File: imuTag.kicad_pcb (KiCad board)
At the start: 4 copper layers, 41.3 x 40 mm, 44 parts, among them J1 Conn_02x05_Odd_Even, J3 Conn_01x02_Pin, Q1 DMG2305UX-13, U1 E73-2G4M08S1C, U2 ME6211C30M5G-N, U3 GD25Q64ESIG, U4 LSM6DSV16XTR, U5 LIS2MDLTR, Y2 Crystal

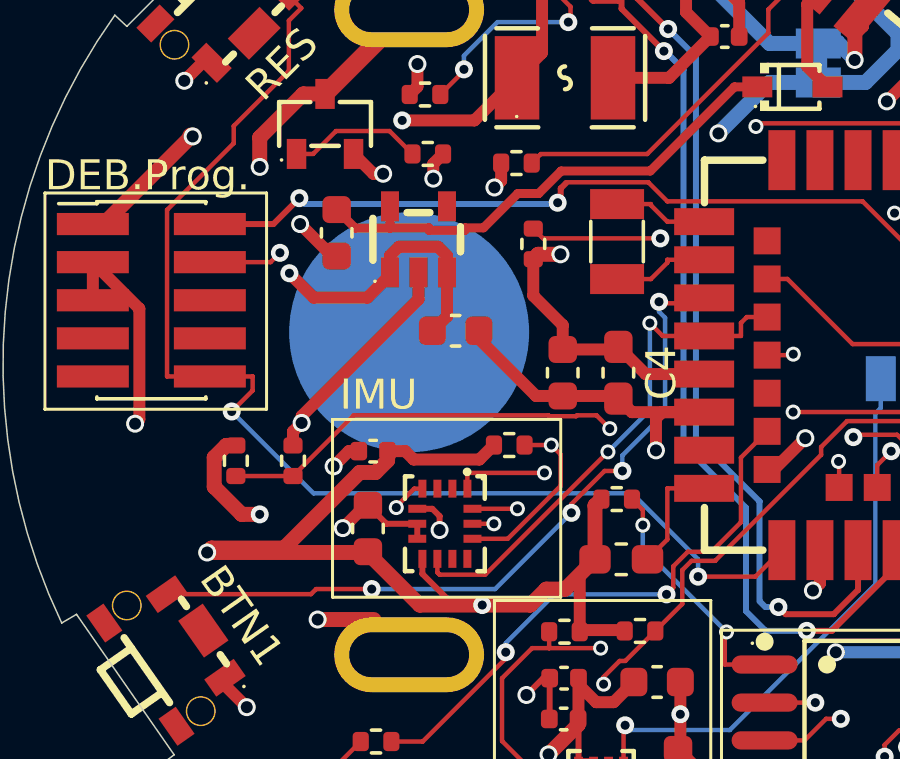
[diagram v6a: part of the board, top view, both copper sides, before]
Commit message: Add 32 kHz crystal and load capacitors
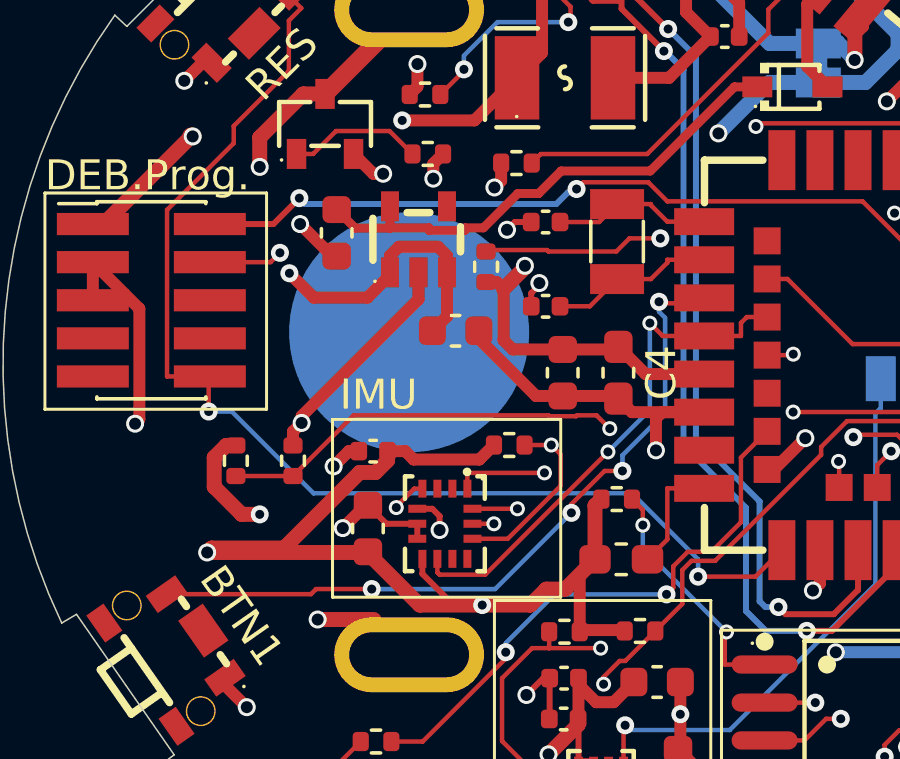
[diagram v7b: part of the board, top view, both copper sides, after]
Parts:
- added C6: 12p, Capacitor_SMD:C_0402_1005Metric, F.Cu at (167.6, 98.2)
- added C7: 12p, Capacitor_SMD:C_0402_1005Metric, F.Cu at (167.6, 95.4)
- moved R15 1.75 mm to (165.6, 96.9)
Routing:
- net VCC: track 172.9 -> 175.4 mm
- net Net-(U1-XL2): track 3.22 -> 5.50 mm
- net Net-(U1-XL1): track 3.17 -> 5.32 mm
- net GND: track 61.2 -> 63.0 mm, vias 18 -> 20
- net Net-(JP7-B): track 50.9 -> 52.6 mm
- net /RESET: track 40.6 -> 39.7 mm

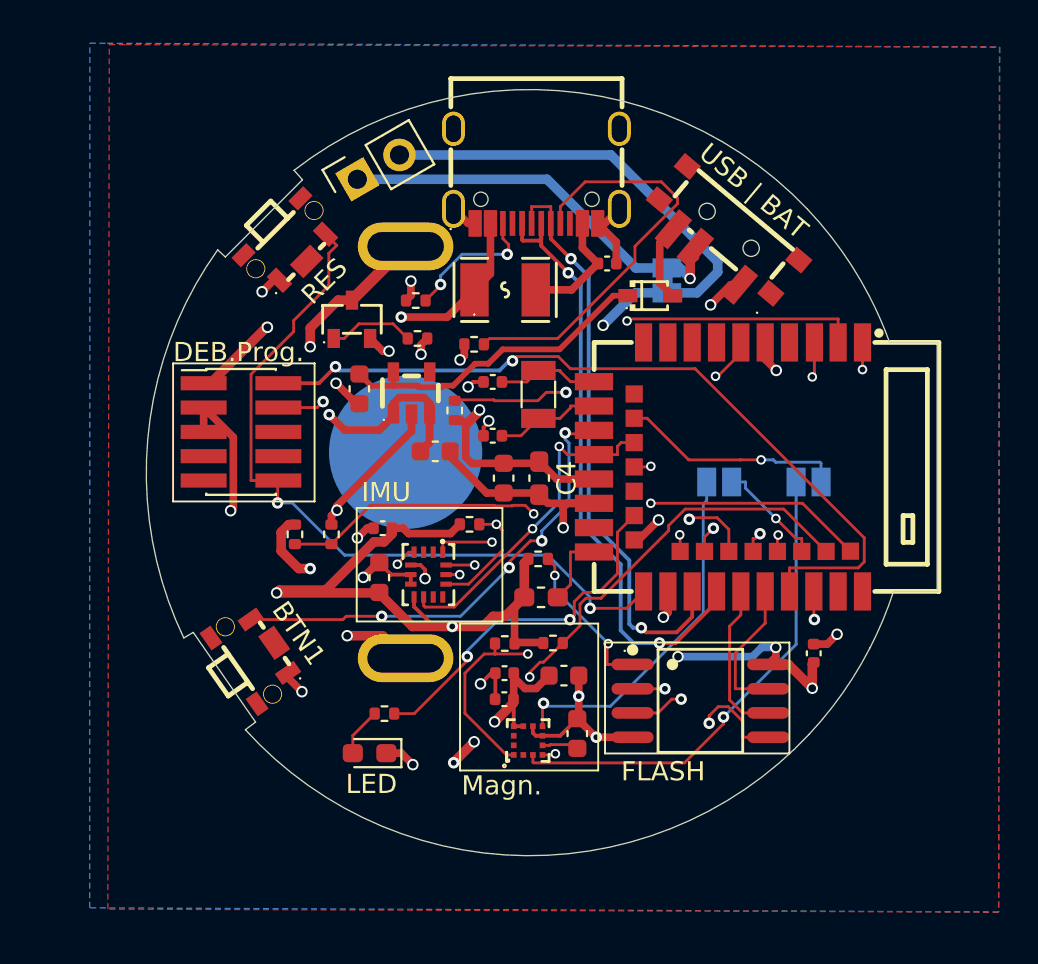
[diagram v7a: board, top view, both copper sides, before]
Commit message: Add debug pins AI0 to AI4 to layout
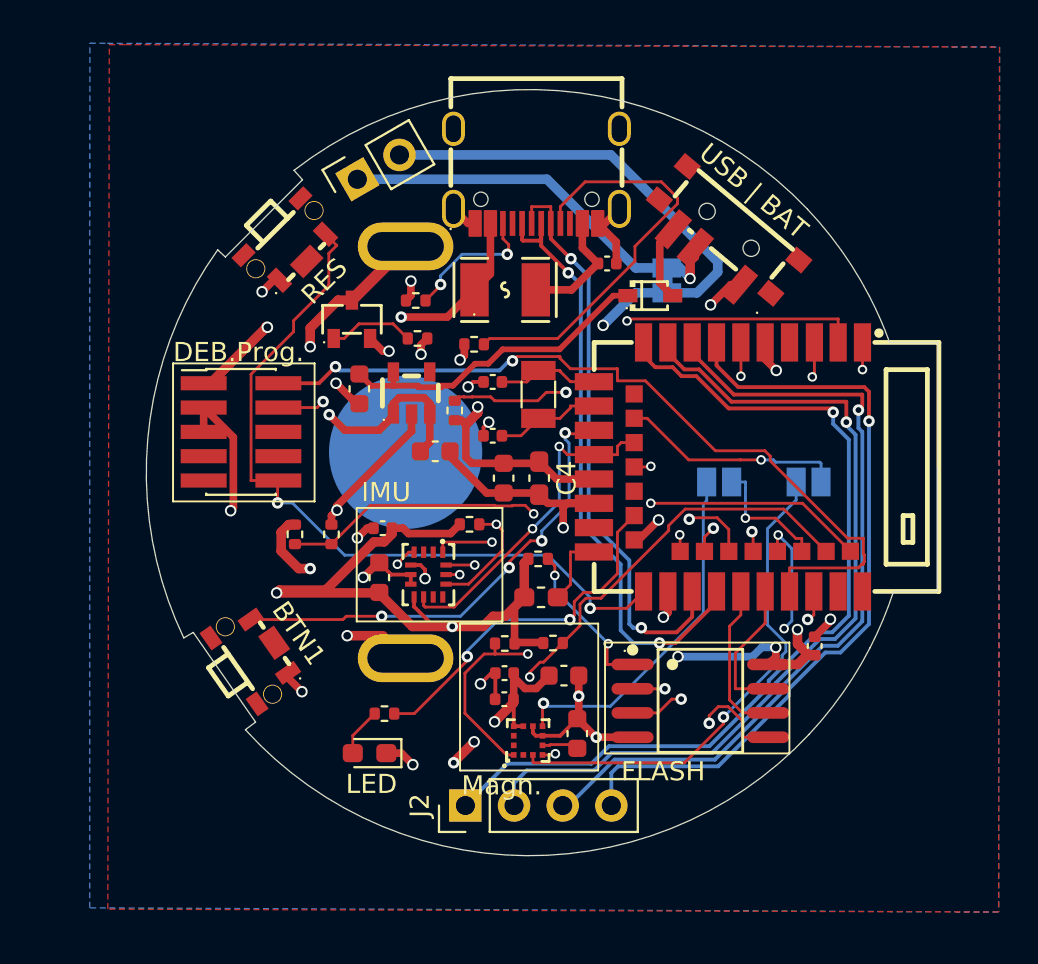
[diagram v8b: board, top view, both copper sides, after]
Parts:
- added J2: Conn_01x04_Pin, Connector_PinHeader_2.54mm:PinHeader_1x04_P2.54mm_Vertical, F.Cu at (166.1, 117.5)
- moved C14 0.38 mm to (184.4, 109.2)
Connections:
- U1 pad 10: unconnected-(U1-AI6-Pad10) -> /AI3
- U1 pad 7: unconnected-(U1-AI0-Pad7) -> /AI0
- U1 pad 8: unconnected-(U1-AI5-Pad8) -> /AI1
- U1 pad 9: unconnected-(U1-AI7-Pad9) -> /AI2
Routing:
- net /AI3: track 0.00 -> 47.2 mm, vias 0 -> 1
- net /AI2: track 0.00 -> 45.2 mm, vias 0 -> 1
- net /AI1: track 0.00 -> 42.1 mm, vias 0 -> 1
- net /AI0: track 0.00 -> 40.4 mm, vias 0 -> 1
- net VCC: track 175.4 -> 178.5 mm
- net /SWDCLK: track 42.4 -> 43.7 mm
- net /LSM6DSV16_INT1: track 42.0 -> 40.9 mm, vias 2 -> 3
- net Net-(JP7-B): track 52.6 -> 53.5 mm
- net /LIS2MDL_INT: track 5.75 -> 6.67 mm
- net /SPI1_MISO: track 23.8 -> 24.5 mm
- net /SWDIO: track 41.8 -> 42.3 mm
